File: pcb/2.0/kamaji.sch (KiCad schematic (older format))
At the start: 37 parts, among them J1 RJ10, J2 RJ10, J3 RJ10, J4 RJ10, J5 RJ10, Q1 IRF540N, SW1 CTRL1, SW2 CTRL2, SW3 CTRL3, U1 ATmega32U4, Y1 Crystal

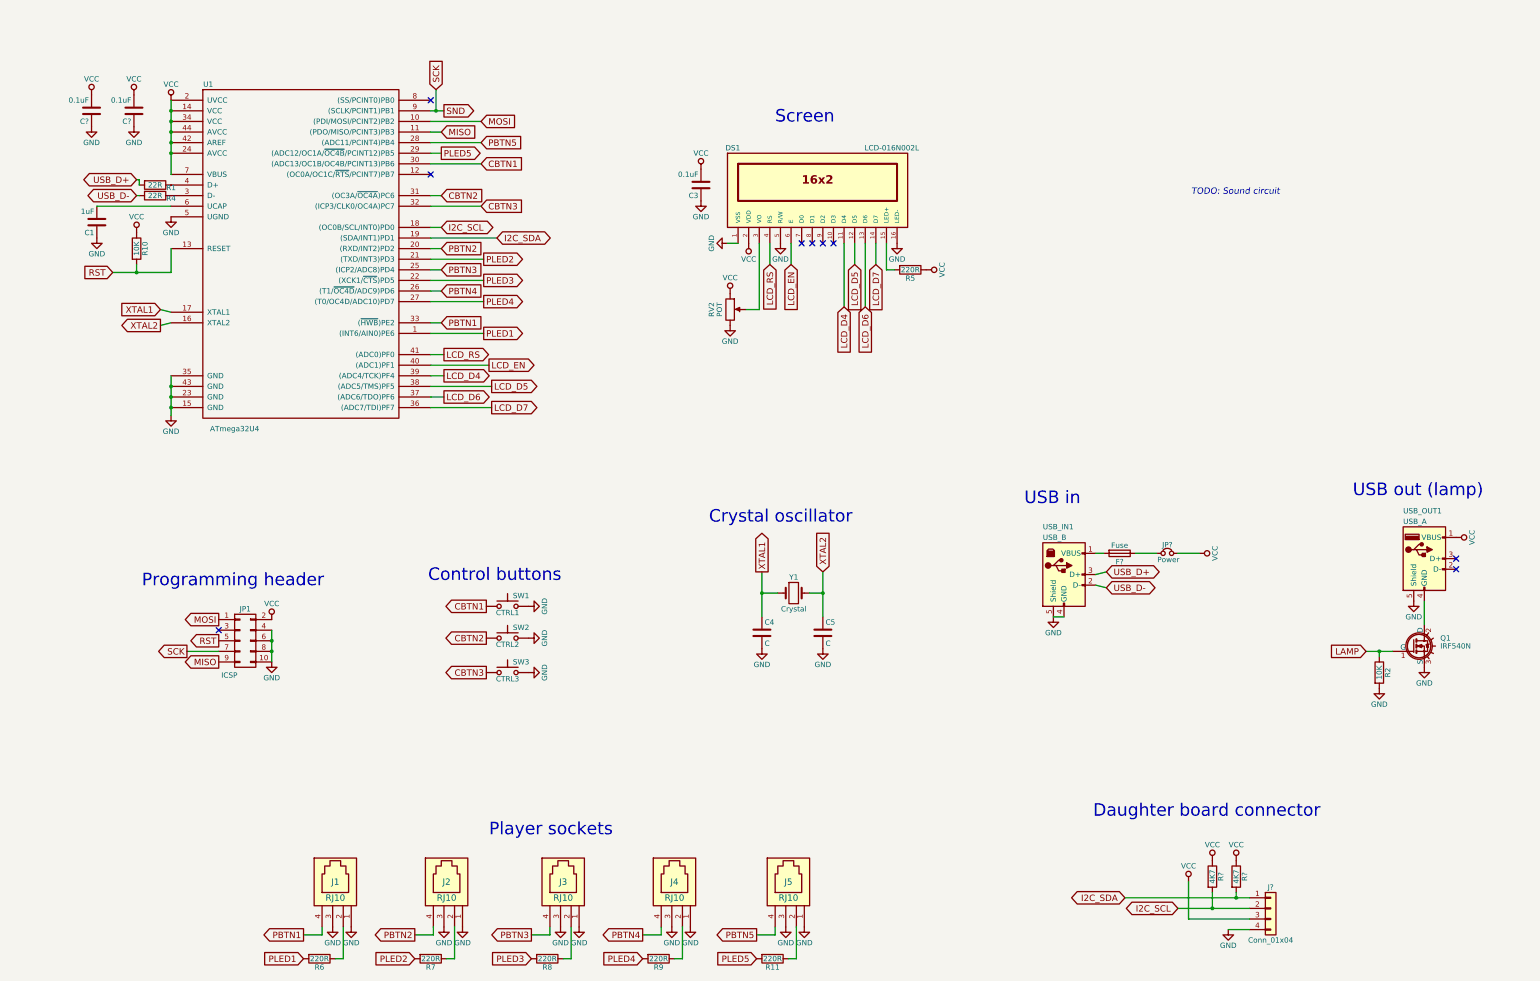
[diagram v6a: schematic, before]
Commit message: start the 2.0 schematic from scratch
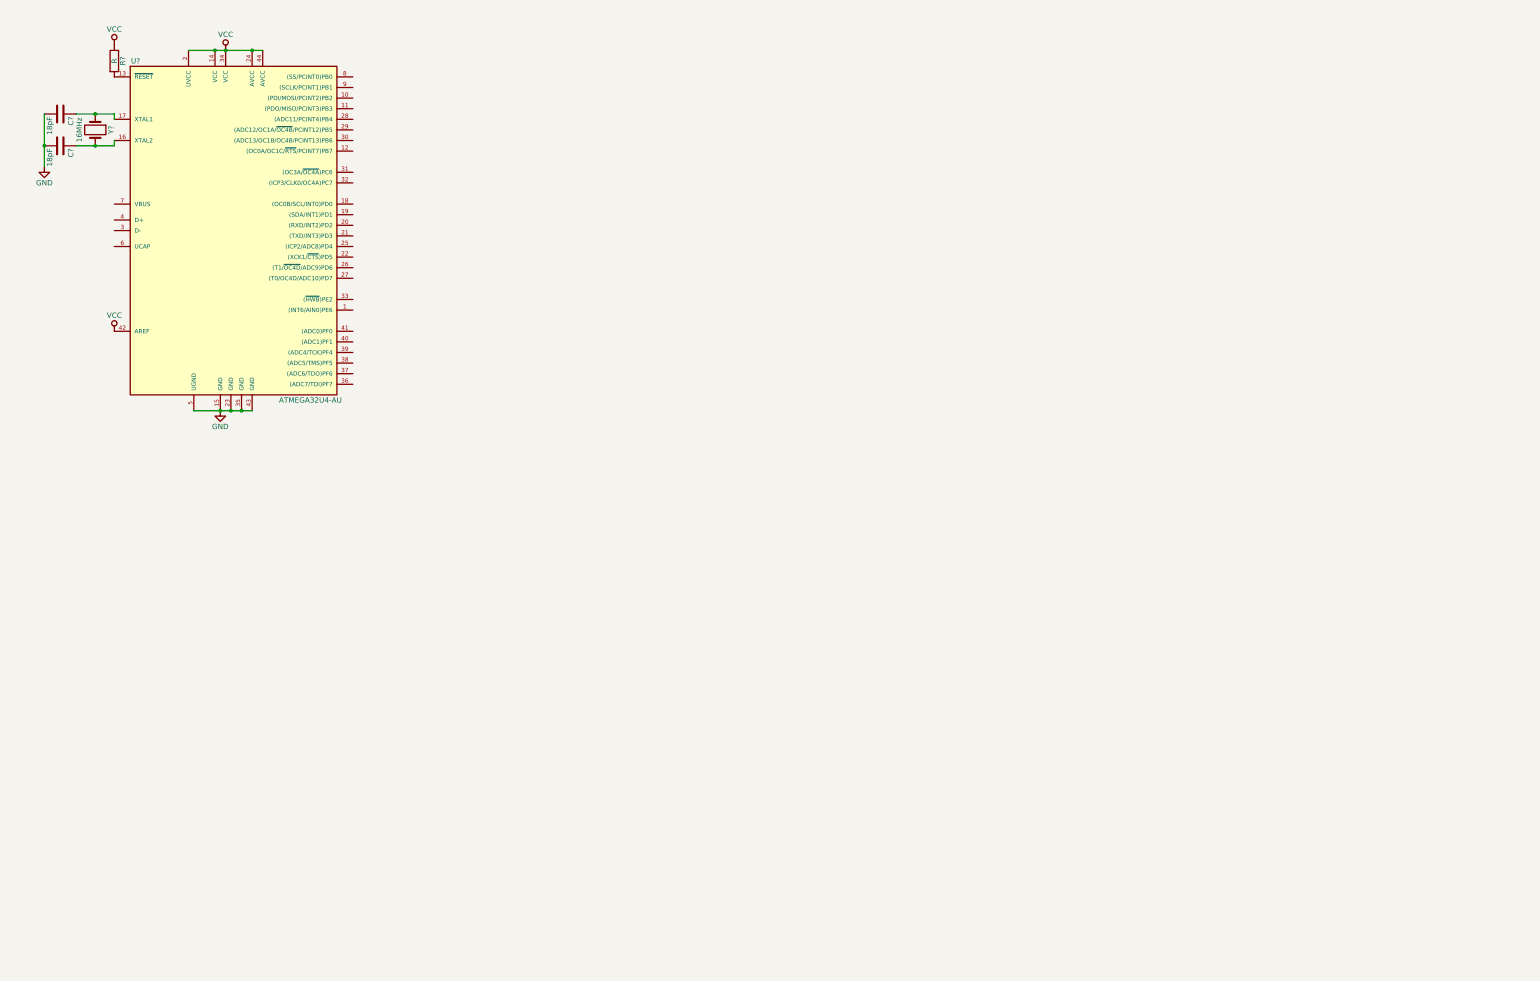
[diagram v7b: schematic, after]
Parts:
- removed C1: 1uF, Capacitors_THT:C_Disc_D3.8mm_W2.6mm_P2.50mm, symbol C
- removed C3, C? (x2): 0.1uF, Capacitors_THT:C_Disc_D3.8mm_W2.6mm_P2.50mm, symbol C
- removed C4, C5: C, Capacitors_THT:C_Disc_D3.8mm_W2.6mm_P2.50mm, symbol C
- removed DS1: LCD-016N002L, Displays:WC1602A, symbol LCD-016N002L-RESCUE-kamaji
- removed F?: Fuse, symbol Fuse
- removed J1, J2, J3, J4, J5: RJ10, kamaji:RJ10, symbol RJ10
- removed J?: Conn_01x04, symbol Conn_01x04
- removed JP1: ICSP, Connectors:IDC_Header_Straight_10pins, symbol CONN_02X05
- removed JP?: Power, symbol Jumper_NC_Small
- removed Q1: IRF540N, TO_SOT_Packages_THT:TO-220_Horizontal, symbol IRF540N-RESCUE-kamaji
- removed R1, R4: 22R, symbol R
- removed R10, R2: 10K, Resistors_THT:R_Axial_DIN0207_L6.3mm_D2.5mm_P10.16mm_Horizontal, symbol R
- removed R11, R5, R6, R7, R8, R9: 220R, Resistors_THT:R_Axial_DIN0207_L6.3mm_D2.5mm_P10.16mm_Horizontal, symbol R
- removed R? (x2): 4K7, symbol R
- removed RV2: POT, Potentiometers:Potentiometer_Triwood_RM-065, symbol POT
- removed SW1: CTRL1, Buttons_Switches_THT:SW_PUSH_6mm_h8.5mm, symbol SW_Push
- removed SW2: CTRL2, Buttons_Switches_THT:SW_PUSH_6mm_h8.5mm, symbol SW_Push
- removed SW3: CTRL3, Buttons_Switches_THT:SW_PUSH_6mm_h8.5mm, symbol SW_Push
- removed U1: ATmega32U4, symbol ATmega32U4
- removed USB_IN1: USB_B, Connectors:USB_B, symbol USB_B
- removed USB_OUT1: USB_A, Connectors:USB_A, symbol USB_A
- removed Y1: Crystal, Crystals:Crystal_HC49-U_Vertical, symbol Crystal
- added C? (x2): 18pF, symbol C
- added R?: R, symbol R
- added U?: ATMEGA32U4-AU, TQFP44, symbol ATMEGA32U4-AU
- added Y?: 16MHz, symbol Crystal
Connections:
- net GND: now also C?.2, C?.2, U?.15 (GND), U?.23 (GND), U?.35 (GND), U?.43 (GND), U?.5 (UGND)
- net VCC: now also R?.1, U?.14 (VCC), U?.2 (UVCC), U?.24 (AVCC), U?.34 (VCC), U?.42 (AREF), U?.44 (AVCC)
- new net: R?.2, U?.13 (~RESET~)
- new net: C?.1, U?.16 (XTAL2), Y?.2
- new net: C?.1, U?.17 (XTAL1), Y?.1
- no-connect marks 9 -> 0
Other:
- note removed: "Control buttons"
- note removed: "Crystal oscillator"
- note removed: "Daughter board connector"
- note removed: "Player sockets"
- note removed: "Programming header"
- note removed: "Screen"
- note removed: "TODO: Sound circuit"
- note removed: "USB in"
- note removed: "USB out (lamp)"

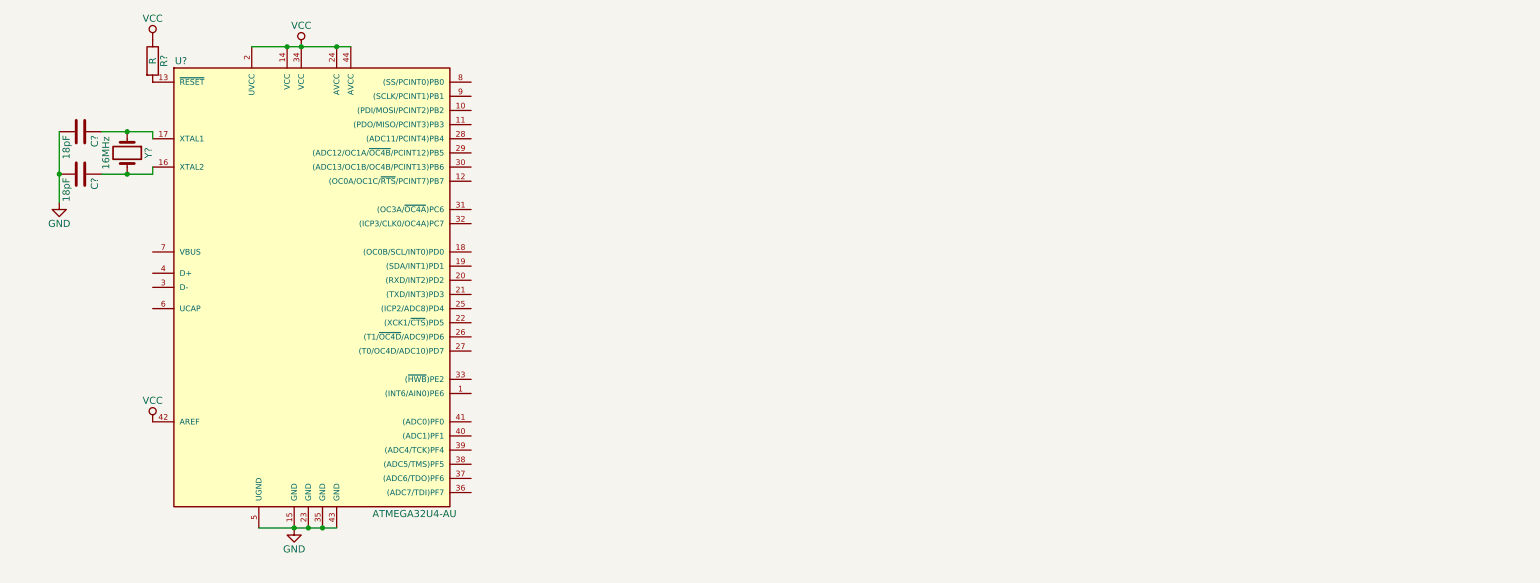
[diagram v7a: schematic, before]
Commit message: psb: add screen, sound, usb, dummy load and ICSP
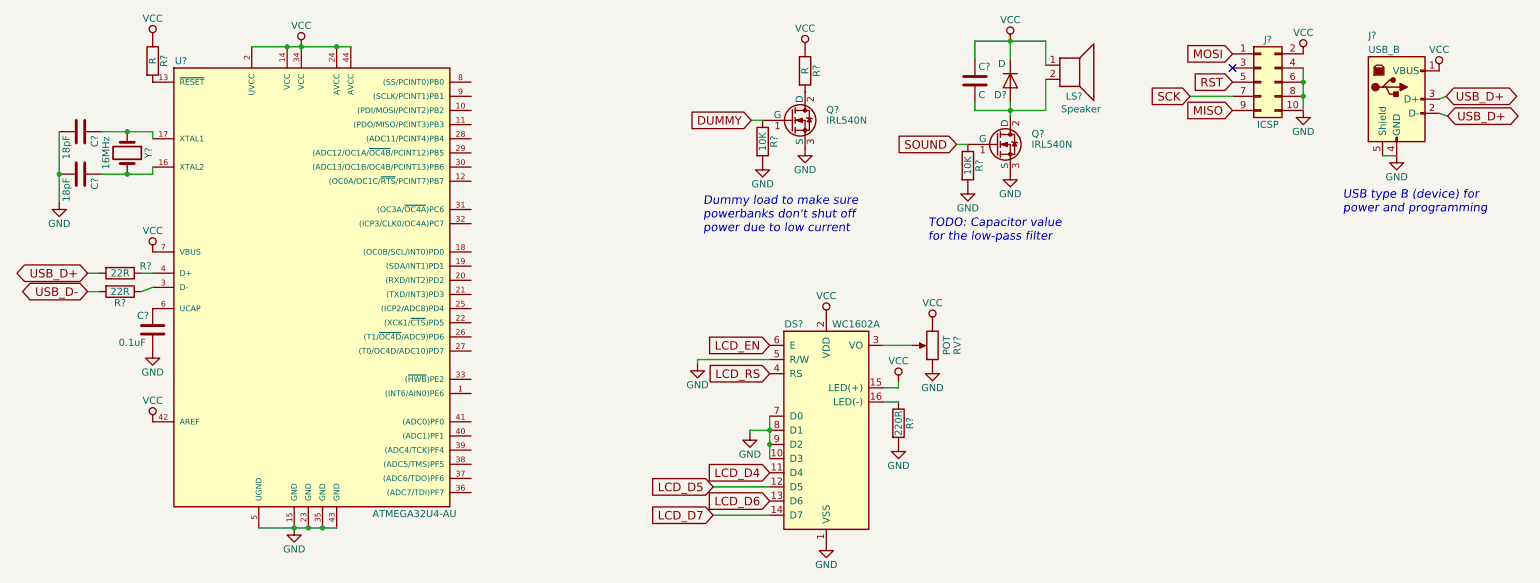
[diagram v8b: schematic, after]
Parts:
- added C?: 0.1uF, symbol C
- added C?: C, symbol C
- added D?: D, symbol D
- added DS?: WC1602A, Displays:WC1602A, symbol WC1602A
- added J?: ICSP, symbol Conn_02x05_Odd_Even
- added J?: USB_B, symbol USB_B
- added LS?: Speaker, symbol Speaker
- added Q? (x2): IRL540N, TO_SOT_Packages_THT:TO-220_Vertical, symbol IRLIZ44N
- added R? (x2): 22R, symbol R
- added R?: R, symbol R
- added R? (x2): 10K, symbol R
- added R?: 220R, symbol R
- added RV?: POT, symbol POT
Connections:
- net GND: now also C?.2, DS?.1 (VSS), DS?.10 (D3), DS?.5 (R/W), DS?.7 (D0), DS?.8 (D1), DS?.9 (D2), J?.10 (Pin_10), J?.4 (GND), J?.4 (Pin_4), J?.5 (Shield), J?.6 (Pin_6), J?.8 (Pin_8), Q?.3 (S), Q?.3 (S), R?.2, R?.2, R?.2, RV?.1
- net VCC: now also U?.7 (VBUS), C?.1, D?.1 (K), DS?.15 (LED(+)), DS?.2 (VDD), J?.1 (VBUS), J?.2 (Pin_2), LS?.1, R?.1, RV?.3
- net at U?.3 (D-): now also R?.1
- net at U?.4 (D+): now also R?.1
- net at U?.6 (UCAP): now also C?.1
- new net: Q?.2 (D), R?.2
- new net: C?.2, D?.2 (A), LS?.2, Q?.2 (D)
- new net: DS?.16 (LED(-)), R?.1
- new net: DS?.3 (VO), RV?.2
- new net DUMMY: Q?.1 (G), R?.1
- new net LCD_D4: DS?.11 (D4)
- new net LCD_D5: DS?.12 (D5)
- new net LCD_D6: DS?.13 (D6)
- new net LCD_D7: DS?.14 (D7)
- new net LCD_EN: DS?.6 (E)
- new net LCD_RS: DS?.4 (RS)
- new net MISO: J?.9 (Pin_9)
- new net MOSI: J?.1 (Pin_1)
- new net RST: J?.5 (Pin_5)
- new net SCK: J?.7 (Pin_7)
- new net SOUND: Q?.1 (G), R?.1
- new net USB_D+: J?.2 (D-), J?.3 (D+), R?.2
- new net USB_D-: R?.2
- no-connect marks 0 -> 1
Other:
- note added: "Dummy load to make sure\npowerbanks don't shut off\npower due to low current"
- note added: "TODO: Capacitor value\nfor the low-pass filter"
- note added: "USB type B (device) for\npower and programming"
